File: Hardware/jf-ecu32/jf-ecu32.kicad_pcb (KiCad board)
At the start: 2 copper layers, 71.4 x 46 mm, 73 parts, among them J1 GAZ, J10 k, J11 RPM, J12 S.PORT, J13 PPM/PWM, J14 PUMP1, J15 PUMP1, J16 PPM/PWM, J17 PUMP2, J18 PUMP2, J19 UART0, J2 AUX, J3 PPM/PWM, J4 STARTER, J5 GLOW, J6 VANNE KEROSTART, J7 VANNE KERO, J8 BATTERY 2S/3S, J9 STARTER, Q1 AO3400A, Q2 QM6006D, Q3 AO3400A, Q4 QM6006D, Q5 QM6006D, Q6 QM6006D, Q7 AO3401A, U1 ESP32-WROOM-32D, U2 4050, U3 MAX31855KASA, U4 AMS1117-3.3, U5 4050, U6 AMS1117-5.0

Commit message: PCB V2
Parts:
- added BOOT0: Conn_01x01_Male, Connector_PinHeader_2.00mm:PinHeader_1x01_P2.00mm_Vertical, F.Cu at (55.4, 183.9)
- added GND2: Conn_01x01_Male, Connector_PinHeader_2.00mm:PinHeader_1x01_P2.00mm_Vertical, F.Cu at (55.4, 186.8)
- GND1, TCK1, TDI1, TDO1, TMS1: footprint Connector_PinHeader_1.00mm:PinHeader_1x01_P1.00mm_Vertical -> Connector_PinHeader_2.00mm:PinHeader_1x01_P2.00mm_Vertical
- moved GND1 1.91 mm to (69.1, 168.4)
- moved C11 1.74 mm to (34.4, 152.0), turned to 180 degrees
- moved TCK1 1.40 mm to (66.9, 168.4)
- moved TDI1 1.20 mm to (47.4, 163.1)
- moved TDO1 0.90 mm to (64.8, 168.4)
- moved TMS1 0.46 mm to (59.7, 164.7)
- moved R14 0.28 mm to (57.0, 176.0)
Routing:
- net Net-(BOOT1-Pad1): track 4.40 -> 21.4 mm, vias 0 -> 3
- net PWM_KERO_3.3: track 40.0 -> 41.1 mm
- net TCK: track 9.49 -> 8.63 mm
- net Net-(D15-Pad2): track 14.3 -> 13.4 mm
- net Net-(D3-Pad2): track 17.7 -> 17.1 mm
- net Net-(D13-Pad2): track 14.4 -> 13.8 mm
- net +5V: track 61.8 -> 61.7 mm, vias 9 -> 8
- net BRAKE: vias 8 -> 7
- net GND: vias 355 -> 361
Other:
- board size 71.4 x 46 mm -> 71.2 x 47 mm

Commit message: PCB V2 Final
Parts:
- moved D13 0.64 mm to (30.7, 186.1)
- moved D3 0.51 mm to (30.5, 179.2)
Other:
- board text added: "3.3V TX RX GND"
- board text added: "AUX"
- board text added: "BATT"
- board text added: "BOOTLOADER"
- board text added: "ESC"
- board text added: "ESC DIRECT"
- board text added: "GL"
- board text added: "GND"
- board text added: "GND 5V SIG"
- board text added: "INPUTS"
- board text added: "IO0"
- board text added: "JF-ECU32 2.0 04-2023"
- board text added: "K"
- board text added: "K+"
- board text added: "K-"
- board text added: "KS"
- board text added: "P1"
- board text added: "P2"
- board text added: "RPM"
- board text added: "S + -"
- board text added: "ST"
- board text added: "TEMP"
- board text added: "TH"
- board text added: "TLM"
- board text added: "UART0"

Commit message: PCB V3
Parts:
- added C4: 0.1µF, Capacitor_SMD:C_0603_1608Metric, B.Cu at (37.1, 178.5)
- added R17: 20K, Resistor_SMD:R_0603_1608Metric, B.Cu at (39.0, 180.8)
- added R18: 100, Resistor_SMD:R_0603_1608Metric, B.Cu at (41.0, 182.8)
- added R19: 7K, Resistor_SMD:R_0603_1608Metric, B.Cu at (41.0, 181.5)
- added R20: 20K, Resistor_SMD:R_0603_1608Metric, B.Cu at (41.0, 180.3)
- added R21: 510K, Resistor_SMD:R_0603_1608Metric, B.Cu at (43.1, 177.6)
- added R22: 500, Resistor_SMD:R_0603_1608Metric, B.Cu at (37.1, 176.7)
- added U7: OPA340NA, Package_TO_SOT_SMD:SOT-23-5, B.Cu at (40.4, 177.6)
- added U8: LM4040DBZ-2.5, Package_TO_SOT_SMD:SOT-23, B.Cu at (36.4, 182.5)
- moved C5 0.38 mm to (44.9, 159.1)
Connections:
- U1 pad 33: RPM -> RPM-2
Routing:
- net RPM-2: track 0.00 -> 36.5 mm, vias 0 -> 1
- net +5V: track 61.7 -> 89.7 mm, vias 8 -> 10
- net RPM: track 54.5 -> 34.0 mm, vias 1 -> 0
- net +2V5: track 0.00 -> 10.8 mm
- net Net-(R20-Pad2): track 0.00 -> 3.43 mm
- net Net-(C4-Pad2): track 0.00 -> 2.92 mm
- net Net-(R18-Pad2): track 0.00 -> 1.30 mm
- net (no net): vias 0 -> 1
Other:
- board text added: "JF-ECU32 3.0 09-2023"
- board text removed: "JF-ECU32 2.0 04-2023"

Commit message: RPM problem
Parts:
- added C12: 0.1µF, Capacitor_SMD:C_0603_1608Metric, B.Cu at (36.4, 179.1)
- R18: value 100 -> 20K
- R19: value 7K -> 20K
- R21: value 510K -> 20K
- moved R21 8.06 mm to (36.3, 182.1), turned to 0 degrees
- moved U8 6.12 mm to (42.5, 181.9), turned to -90 degrees
- moved R20 4.64 mm to (36.4, 180.5), turned to 180 degrees
- moved R17 4.00 mm to (36.4, 177.7), turned to 180 degrees
- moved C4 2.25 mm to (36.5, 176.3), turned to 180 degrees
- moved R19 1.97 mm to (39.3, 180.5), turned to 0 degrees
- moved R18 1.93 mm to (39.3, 182.1), turned to 180 degrees
- moved R22 1.56 mm to (38.6, 177.0), turned to -90 degrees
- moved U7 1.11 mm to (41.4, 178.1)
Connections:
- R18 pad 1: GND -> RPM-2
- R18 pad 2: Net-(R18-Pad2) -> Net-(R21-Pad2)
- R19 pad 1: Net-(R18-Pad2) -> GND
- R19 pad 2: +2V5 -> RPM-2
- R21 pad 2: RPM-2 -> Net-(R21-Pad2)
- U7 pad 1: RPM-2 -> Net-(R21-Pad2)
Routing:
- net Net-(R20-Pad2): track 3.43 -> 16.5 mm, vias 0 -> 5
- net Net-(R21-Pad2): track 0.00 -> 11.6 mm
- net Net-(C4-Pad2): track 2.92 -> 7.72 mm, vias 0 -> 2
- net RPM-2: track 36.5 -> 40.9 mm
- net RPM: track 34.0 -> 31.2 mm
- net Net-(R18-Pad2): track 1.30 -> 0.00 mm
- net +2V5: track 10.8 -> 10.1 mm
- net GND: vias 361 -> 363

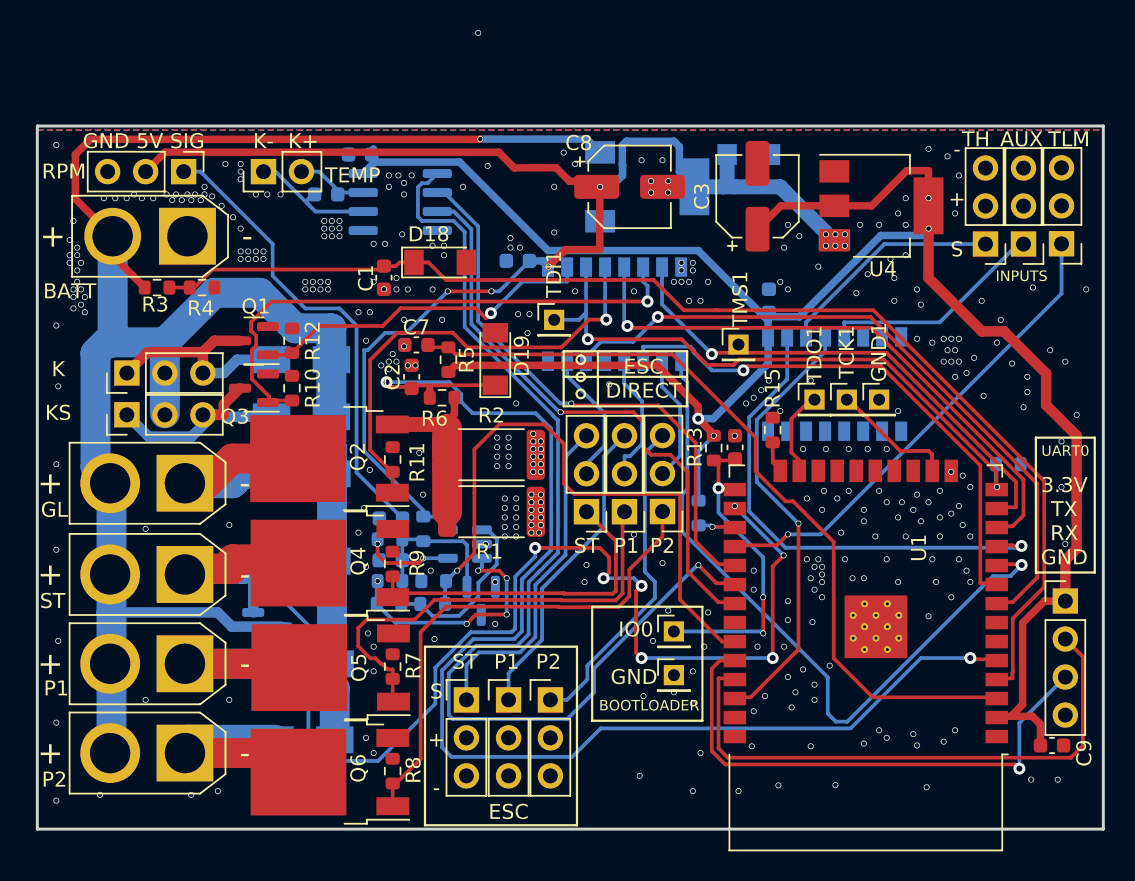
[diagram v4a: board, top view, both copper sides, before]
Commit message: Préparation de la V3
Ajout d'un ampli op pour la lecture des RPM et d'un capteur de courant pour la bougie.
Correction de l'alimentation de la bougie.
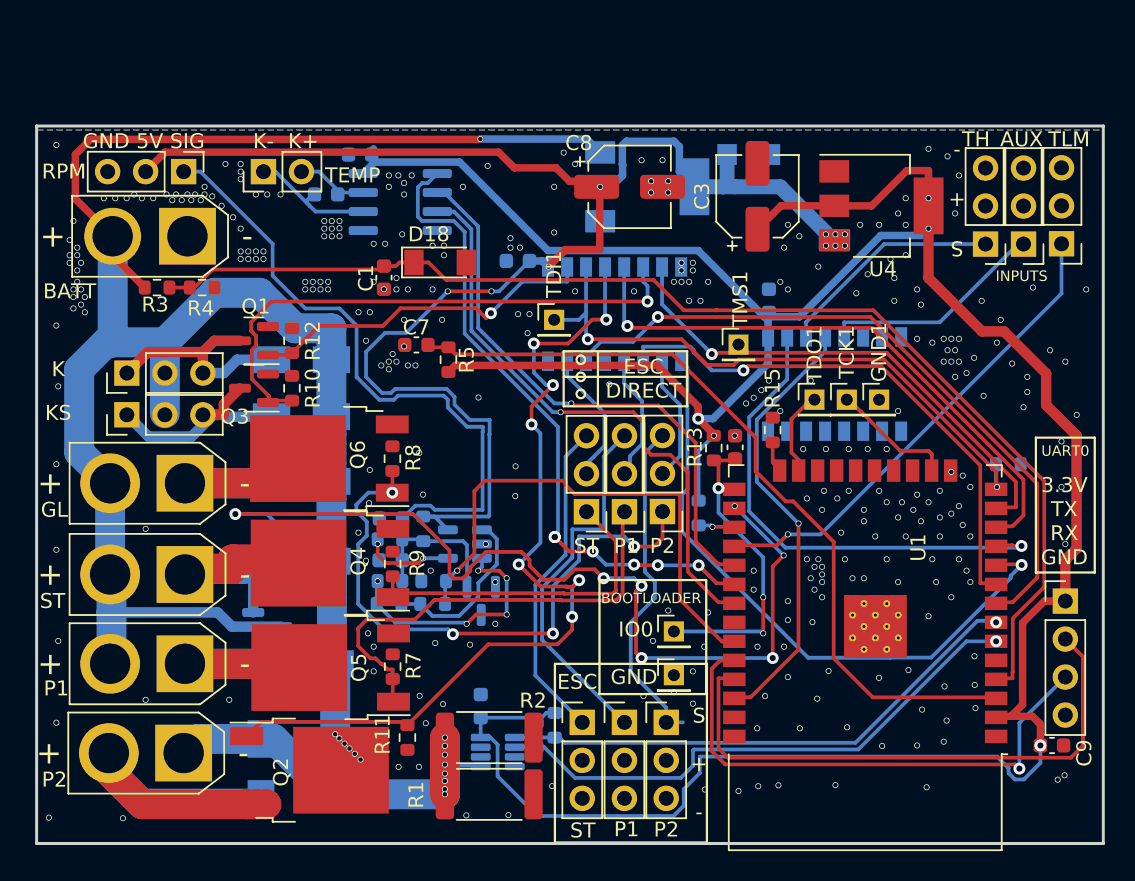
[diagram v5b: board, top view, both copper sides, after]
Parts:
- removed D19: BZV55C3V3, Diode_SMD:D_MiniMELF
- added R23: 1K, Resistor_SMD:R_0603_1608Metric, B.Cu at (46.2, 190.8)
- added U9: INA219AxDCN, Package_TO_SOT_SMD:SOT-23-8, B.Cu at (43.6, 192.0)
- C2: value 10nF -> 0.1µF; moved to B.Cu
- R6: value 10K -> 1K; moved to B.Cu
- moved R6 23.1 mm to (47.4, 190.2), turned to 90 degrees
- moved C2 22.5 mm to (42.5, 188.9)
- moved Q6 21.0 mm to (32.4, 172.3)
- moved R8 20.9 mm to (36.6, 172.3)
- moved Q2 20.9 mm to (31.0, 193.2), turned to 0 degrees
- moved D10 19.9 mm to (27.8, 193.1), turned to 90 degrees
- moved R2 18.9 mm to (43.0, 191.0)
- moved R1 18.9 mm to (43.0, 194.8)
- moved R11 18.6 mm to (37.6, 191.0), turned to -90 degrees
- moved J5 18.0 mm to (22.6, 192.0)
- moved J17 18.0 mm to (22.7, 174.0)
- moved D15 17.3 mm to (30.5, 173.9)
- moved J15 7.89 mm to (52.1, 190.0)
- moved J18 7.89 mm to (54.9, 190.0)
- moved J4 7.89 mm to (49.2, 190.0)
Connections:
- C2 pad 1: GLOW_CURRENT -> 3.3V
- D10 pad 1: +BATT -> Net-(D10-Pad1)
- J5 pad 2: +BATT -> Net-(D10-Pad1)
- Q2 pad 2: Net-(D10-Pad2) -> +BATT
- Q2 pad 3: Net-(Q2-Pad3) -> Net-(D10-Pad1)
- R1 pad 1: Net-(Q2-Pad3) -> Net-(D10-Pad2)
- R2 pad 1: Net-(Q2-Pad3) -> Net-(D10-Pad2)
- R6 pad 1: GLOW_CURRENT -> ESP_SCL
- R6 pad 2: Net-(Q2-Pad3) -> 3.3V
- U1 pad 5: GLOW_CURRENT -> unconnected-(U1-Pad5)
- U1 pad 6: unconnected-(U1-Pad6) -> ESP_SDA
- U1 pad 7: unconnected-(U1-Pad7) -> ESP_SCL
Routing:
- net GLOW_CURRENT: track 86.6 -> 0.00 mm, vias 2 -> 0
- net 3.3V: track 145.6 -> 198.5 mm, vias 4 -> 5
- net ESP_SDA: track 0.00 -> 37.4 mm, vias 0 -> 1
- net ESP_SCL: track 0.00 -> 35.7 mm, vias 0 -> 1
- net PWM_GLOW: track 30.8 -> 59.3 mm, vias 1 -> 7
- net CLK: track 71.6 -> 43.6 mm, vias 1 -> 6
- net Net-(D10-Pad1): track 0.00 -> 25.1 mm
- net Net-(D10-Pad2): track 14.4 -> 29.3 mm, vias 0 -> 8
- net Net-(Q2-Pad3): track 11.2 -> 0.00 mm
- net RPM: track 31.2 -> 42.2 mm
- net +5V: track 90.1 -> 99.8 mm
- net Net-(J16-Pad1): track 34.1 -> 40.3 mm, vias 0 -> 4
- net RPM-2: track 40.9 -> 34.7 mm
- net PPM_PWM_PUMP2_3.3: track 47.1 -> 42.3 mm
- net BRAKE: track 71.5 -> 67.1 mm
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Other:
- board size 71.2 x 47 mm -> 71.3 x 48 mm
- board text added: "JF-ECU32 3.0 08-2024"
- board text removed: "JF-ECU32 3.0 09-2023"

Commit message: Correction des erreur de PCB
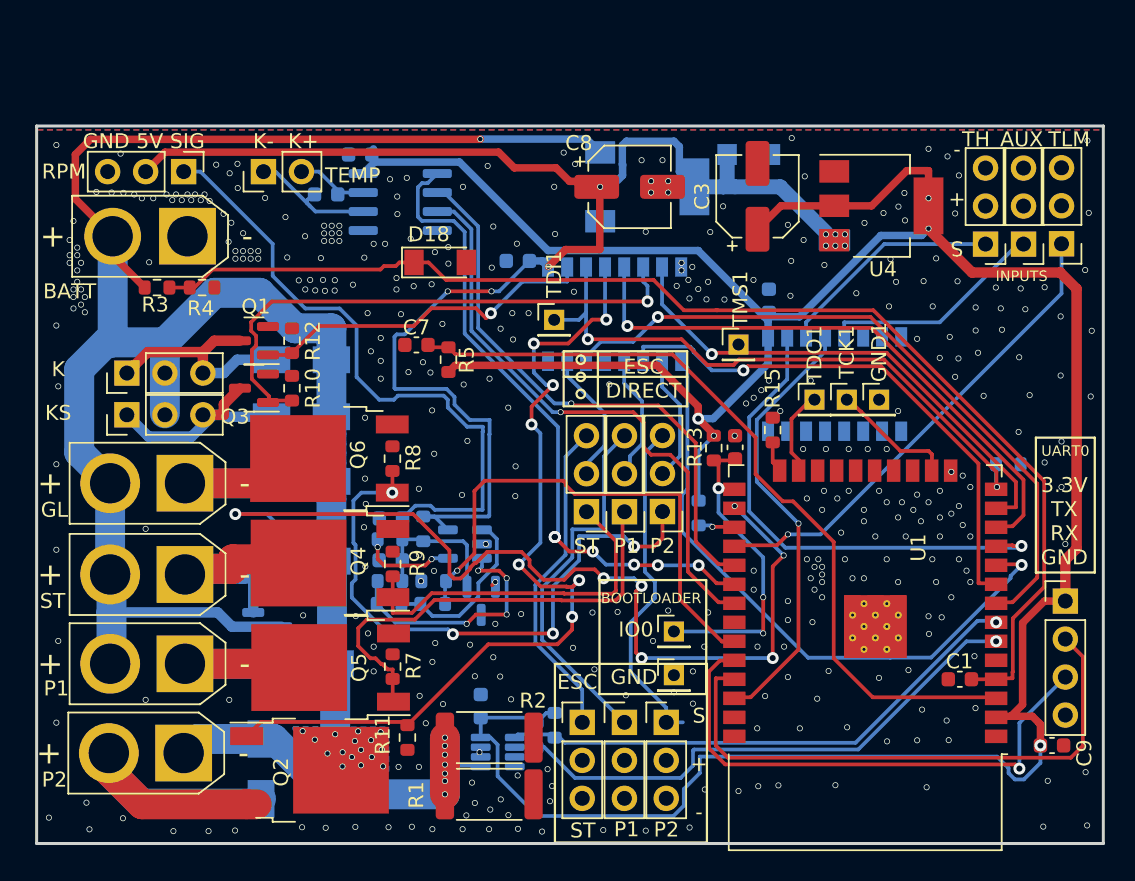
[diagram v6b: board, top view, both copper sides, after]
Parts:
- moved C1 46.9 mm to (74.5, 187.1), turned to 180 degrees
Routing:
- net +5V: track 99.8 -> 96.8 mm
- net 3.3V: track 198.5 -> 201.1 mm
- net +BATT: track 139.1 -> 136.7 mm, vias 7 -> 17
- net Net-(J3-Pad1): track 22.5 -> 24.4 mm
- net VBAT_ADC: track 80.5 -> 82.1 mm
- net Net-(D10-Pad1): track 25.1 -> 24.4 mm
- net GND: track 0.00 -> 0.30 mm, vias 323 -> 375
- net Net-(R20-Pad2): vias 5 -> 4
- net Net-(D10-Pad2): vias 8 -> 7
- added copper zone on B.Cu, net +BATT
